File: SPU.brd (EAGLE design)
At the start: 160 x 130 mm, 396 parts, among them Q2 CSTCR6M00G53Z

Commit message: Before autoroute
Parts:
- removed STAMP1:ADC_SG1, STAMP1:ADC_SG2, STAMP1:ADC_TEMP, STAMP2:ADC_SG1, STAMP2:ADC_SG2, STAMP2:ADC_TEMP, STAMP3:ADC_SG1, STAMP3:ADC_SG2, STAMP3:ADC_TEMP, STAMP4:ADC_SG1, STAMP4:ADC_SG2, STAMP4:ADC_TEMP, STAMP5:ADC_SG1, STAMP5:ADC_SG2, STAMP5:ADC_TEMP, STAMP6:ADC_SG1, STAMP6:ADC_SG2, STAMP6:ADC_TEMP: ADS1148QPWRQ1, ads11xx:TSSOP28
- removed STAMP1:C28, STAMP1:C30, STAMP1:C31, STAMP1:C32, STAMP1:C33, STAMP1:C45, STAMP1:C47, STAMP1:C48, STAMP1:C49, STAMP1:C50, STAMP1:C51, STAMP1:C52, STAMP2:C28, STAMP2:C30, STAMP2:C31, STAMP2:C32, STAMP2:C33, STAMP2:C45, STAMP2:C47, STAMP2:C48, STAMP2:C49, STAMP2:C50, STAMP2:C51, STAMP2:C52, STAMP3:C28, STAMP3:C30, STAMP3:C31, STAMP3:C32, STAMP3:C33, STAMP3:C45, STAMP3:C47, STAMP3:C48, STAMP3:C49, STAMP3:C50, STAMP3:C51, STAMP3:C52, STAMP4:C28, STAMP4:C30, STAMP4:C31, STAMP4:C32, STAMP4:C33, STAMP4:C45, STAMP4:C47, STAMP4:C48, STAMP4:C49, STAMP4:C50, STAMP4:C51, STAMP4:C52, STAMP5:C28, STAMP5:C30, STAMP5:C31, STAMP5:C32, STAMP5:C33, STAMP5:C45, STAMP5:C47, STAMP5:C48, STAMP5:C49, STAMP5:C50, STAMP5:C51, STAMP5:C52, STAMP6:C28, STAMP6:C30, STAMP6:C31, STAMP6:C32, STAMP6:C33, STAMP6:C45, STAMP6:C47, STAMP6:C48, STAMP6:C49, STAMP6:C50, STAMP6:C51, STAMP6:C52: 100n, rcl:C0805
- removed STAMP1:C29, STAMP1:C46, STAMP1:C56, STAMP2:C29, STAMP2:C46, STAMP2:C56, STAMP3:C29, STAMP3:C46, STAMP3:C56, STAMP4:C29, STAMP4:C46, STAMP4:C56, STAMP5:C29, STAMP5:C46, STAMP5:C56, STAMP6:C29, STAMP6:C46, STAMP6:C56: 1u, rcl:C0805
- removed STAMP1:C53, STAMP1:C55, STAMP2:C53, STAMP2:C55, STAMP3:C53, STAMP3:C55, STAMP4:C53, STAMP4:C55, STAMP5:C53, STAMP5:C55, STAMP6:C53, STAMP6:C55: 6n8, rcl:C0805
- removed STAMP1:C54, STAMP2:C54, STAMP3:C54, STAMP4:C54, STAMP5:C54, STAMP6:C54: 68n, rcl:C0805
- removed STAMP1:C57, STAMP2:C57, STAMP3:C57, STAMP4:C57, STAMP5:C57, STAMP6:C57: 33n, rcl:C0805
- removed STAMP1:C58, STAMP1:C59, STAMP2:C58, STAMP2:C59, STAMP3:C58, STAMP3:C59, STAMP4:C58, STAMP4:C59, STAMP5:C58, STAMP5:C59, STAMP6:C58, STAMP6:C59: 3n3, rcl:C0805
- removed STAMP1:CON, STAMP2:CON, STAMP3:CON, STAMP4:CON, STAMP5:CON, STAMP6:CON: IL-AG5-10P-S3T2, con-jae:IL-AG5-10P-S3T2
- removed STAMP1:R24, STAMP1:R68, STAMP1:R77, STAMP2:R24, STAMP2:R68, STAMP2:R77, STAMP3:R24, STAMP3:R68, STAMP3:R77, STAMP4:R24, STAMP4:R68, STAMP4:R77, STAMP5:R24, STAMP5:R68, STAMP5:R77, STAMP6:R24, STAMP6:R68, STAMP6:R77: 4k7, rcl:R0805
- removed STAMP1:R29, STAMP1:R32, STAMP1:R72, STAMP1:R73, STAMP2:R29, STAMP2:R32, STAMP2:R72, STAMP2:R73, STAMP3:R29, STAMP3:R32, STAMP3:R72, STAMP3:R73, STAMP4:R29, STAMP4:R32, STAMP4:R72, STAMP4:R73, STAMP5:R29, STAMP5:R32, STAMP5:R72, STAMP5:R73, STAMP6:R29, STAMP6:R32, STAMP6:R72, STAMP6:R73: 40 1%, rcl:R0805
- removed STAMP1:R30, STAMP1:R33, STAMP1:R69, STAMP1:R74, STAMP2:R30, STAMP2:R33, STAMP2:R69, STAMP2:R74, STAMP3:R30, STAMP3:R33, STAMP3:R69, STAMP3:R74, STAMP4:R30, STAMP4:R33, STAMP4:R69, STAMP4:R74, STAMP5:R30, STAMP5:R33, STAMP5:R69, STAMP5:R74, STAMP6:R30, STAMP6:R33, STAMP6:R69, STAMP6:R74: 1k 0.1%, rcl:R0805
- removed STAMP1:R31, STAMP1:R70, STAMP1:R75, STAMP2:R31, STAMP2:R70, STAMP2:R75, STAMP3:R31, STAMP3:R70, STAMP3:R75, STAMP4:R31, STAMP4:R70, STAMP4:R75, STAMP5:R31, STAMP5:R70, STAMP5:R75, STAMP6:R31, STAMP6:R70, STAMP6:R75: 47, rcl:R0805
- removed STAMP1:R78, STAMP1:R79, STAMP2:R78, STAMP2:R79, STAMP3:R78, STAMP3:R79, STAMP4:R78, STAMP4:R79, STAMP5:R78, STAMP5:R79, STAMP6:R78, STAMP6:R79: 4k7 1%, rcl:R0805
- removed STAMP1:R80, STAMP1:R81, STAMP2:R80, STAMP2:R81, STAMP3:R80, STAMP3:R81, STAMP4:R80, STAMP4:R81, STAMP5:R80, STAMP5:R81, STAMP6:R80, STAMP6:R81: 9k09 1%, rcl:R0805
- removed STAMP1:R82, STAMP2:R82, STAMP3:R82, STAMP4:R82, STAMP5:R82, STAMP6:R82: 820 0.1%, rcl:R0805
- removed STAMP1:U$6, STAMP1:U$7, STAMP2:U$6, STAMP2:U$7, STAMP3:U$6, STAMP3:U$7, STAMP4:U$6, STAMP4:U$7, STAMP5:U$6, STAMP5:U$7, STAMP6:U$6, STAMP6:U$7: COMMON_MODE_CHOKE, selfmade:COMMON_MODE_CHOKE
- removed U$1: FT2232D, smf2:FTDI2232D
- removed U$3: M93C46-WDW6TP, smf2:TSSOP-8
- removed U$4: S70FL01GSAGM, smf2:SOIC16
- added C100, C101, C102, C103, C104, C105, C113, C115, C116, C117, C118, C119, C121, C122, C123, C124, C125, C126, C134, C136, C137, C138, C139, C140, C142, C143, C144, C145, C146, C147, C155, C157, C158, C159, C160, C161, C163, C164, C165, C166, C167, C168, C197, C199, C200, C201, C202, C203, C205, C206, C207, C208, C209, C210, C33, C45, C46, C47, C48, C49, C51, C52, C53, C54, C55, C56, C92, C94, C95, C96, C97, C98: 100n, rcl:C0805
- added C106, C108, C127, C129, C148, C150, C169, C171, C211, C213, C57, C59: 6n8, rcl:C0805
- added C107, C128, C149, C170, C212, C58: 68n, rcl:C0805
- added C109, C114, C120, C130, C135, C141, C151, C156, C162, C172, C198, C204, C214, C34, C50, C63, C93, C99: 1u, rcl:C0805
- added C110, C131, C152, C173, C215, C68: 33n, rcl:C0805
- added C111, C112, C132, C133, C153, C154, C174, C175, C216, C217, C69, C70: 3n3, rcl:C0805
- added CON_STAMP1, CON_STAMP3, CON_STAMP4, CON_STAMP5, CON_STAMP6, CON_STAMP8: IL-AG5-10P-S3T2, con-jae:IL-AG5-10P-S3T2
- added FTDI: FT2232D, smf2:FTDI2232D
- added FT_EEPROM: M93C46-WDW6TP, smf2:TSSOP-8
- added R100, R106, R113, R119, R125, R132, R138, R144, R151, R176, R182, R189, R28, R68, R71, R77, R87, R94: 4k7, rcl:R0805
- added R101, R105, R107, R111, R120, R124, R126, R130, R139, R143, R145, R149, R177, R181, R183, R187, R30, R33, R69, R74, R76, R86, R88, R92: 1k 0.1%, rcl:R0805
- added R102, R108, R112, R121, R127, R131, R140, R146, R150, R178, R184, R188, R31, R70, R75, R83, R89, R93: 47, rcl:R0805
- added R103, R104, R109, R110, R122, R123, R128, R129, R141, R142, R147, R148, R179, R180, R185, R186, R29, R32, R72, R73, R84, R85, R90, R91: 40 1%, rcl:R0805
- added R114, R115, R133, R134, R152, R153, R190, R191, R78, R79, R95, R96: 4k7 1%, rcl:R0805
- added R116, R117, R135, R136, R154, R155, R192, R193, R80, R81, R97, R98: 9k09 1%, rcl:R0805
- added R118, R137, R156, R194, R82, R99: 820 0.1%, rcl:R0805
- added S70FL: S70FL01GSAGM, smf2:SOIC16
- added STAMP1_ADC_SG1, STAMP1_ADC_SG10, STAMP1_ADC_SG11, STAMP1_ADC_SG12, STAMP1_ADC_SG15, STAMP1_ADC_SG16, STAMP1_ADC_SG2, STAMP1_ADC_SG5, STAMP1_ADC_SG6, STAMP1_ADC_SG7, STAMP1_ADC_SG8, STAMP1_ADC_SG9, STAMP1_ADC_TEMP, STAMP1_ADC_TEMP2, STAMP1_ADC_TEMP3, STAMP1_ADC_TEMP4, STAMP1_ADC_TEMP5, STAMP1_ADC_TEMP7: ADS1148QPWRQ1, ads11xx:TSSOP28
- added U$10, U$11, U$12, U$13, U$14, U$15, U$16, U$19, U$20, U$6, U$7, U$9: COMMON_MODE_CHOKE, selfmade:COMMON_MODE_CHOKE
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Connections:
- removed net STAMP1:N$34: STAMP1:ADC_SG1.9, STAMP1:C29.1
- removed net STAMP1:N$35: STAMP1:ADC_SG2.4, STAMP1:R68.1
- removed net STAMP1:N$37: STAMP1:ADC_SG1.4, STAMP1:R24.1
- removed net STAMP1:N$38: STAMP1:ADC_SG1.26, STAMP1:R31.2
- removed net STAMP1:N$39: STAMP1:ADC_SG1.11, STAMP1:C31.2, STAMP1:C32.1, STAMP1:R29.1
- removed net STAMP1:N$40: STAMP1:ADC_SG1.12, STAMP1:C32.2, STAMP1:C33.1, STAMP1:R32.1
- removed net STAMP1:N$41: STAMP1:ADC_SG2.9, STAMP1:C46.1
- removed net STAMP1:N$43: STAMP1:ADC_SG2.26, STAMP1:R70.2
- removed net STAMP1:N$79: STAMP1:ADC_SG2.11, STAMP1:C48.2, STAMP1:C49.1, STAMP1:R72.1
- removed net STAMP1:N$80: STAMP1:ADC_SG2.12, STAMP1:C49.2, STAMP1:C50.1, STAMP1:R73.1
- removed net STAMP1:N$81: STAMP1:R30.1, STAMP1:R32.2, STAMP1:R33.1
- removed net STAMP1:N$82: STAMP1:R69.1, STAMP1:R73.2, STAMP1:R74.1
- removed net STAMP1:N$83: STAMP1:R29.2, STAMP1:U$6.P$3
- removed net STAMP1:N$84: STAMP1:R72.2, STAMP1:U$7.P$3
- removed net STAMP1:N$86: STAMP1:ADC_TEMP.26, STAMP1:R75.2
- removed net STAMP1:N$87: STAMP1:ADC_TEMP.4, STAMP1:R77.1
- removed net STAMP1:N$88: STAMP1:ADC_TEMP.12, STAMP1:C53.2, STAMP1:C54.1, STAMP1:R78.1
- removed net STAMP1:N$89: STAMP1:ADC_TEMP.17, STAMP1:C54.2, STAMP1:C55.1, STAMP1:R79.1
- removed net STAMP1:N$90: STAMP1:ADC_TEMP.9, STAMP1:C56.1
- removed net STAMP1:N$91: STAMP1:ADC_TEMP.6, STAMP1:C57.2, STAMP1:C58.1, STAMP1:R81.1
- removed net STAMP1:N$92: STAMP1:ADC_TEMP.5, STAMP1:C57.1, STAMP1:C59.2, STAMP1:R80.1
- removed net STAMP1:SG1_AIN1: STAMP1:CON.P$1, STAMP1:U$6.P$6
- removed net STAMP1:SG1_AIN2: STAMP1:CON.P$2, STAMP1:U$6.P$4
- removed net STAMP1:SG1_AIN3: STAMP1:CON.P$3, STAMP1:U$6.P$2
- removed net STAMP1:SG2_AIN1: STAMP1:CON.P$10, STAMP1:U$7.P$6
- removed net STAMP1:SG2_AIN2: STAMP1:CON.P$9, STAMP1:U$7.P$4
- removed net STAMP1:SG2_AIN3: STAMP1:CON.P$8, STAMP1:U$7.P$2
- removed net STAMP1:TEMP_AIN1: STAMP1:ADC_TEMP.11, STAMP1:CON.P$4, STAMP1:R78.2
- removed net STAMP1:TEMP_AIN2: STAMP1:ADC_TEMP.18, STAMP1:CON.P$5, STAMP1:R79.2
- removed net STAMP1:TEMP_AIN3: STAMP1:CON.P$7, STAMP1:R80.2, STAMP1:R82.2
- removed net STAMP2:N$34: STAMP2:ADC_SG1.9, STAMP2:C29.1
- removed net STAMP2:N$35: STAMP2:ADC_SG2.4, STAMP2:R68.1
- removed net STAMP2:N$37: STAMP2:ADC_SG1.4, STAMP2:R24.1
- removed net STAMP2:N$38: STAMP2:ADC_SG1.26, STAMP2:R31.2
- removed net STAMP2:N$39: STAMP2:ADC_SG1.11, STAMP2:C31.2, STAMP2:C32.1, STAMP2:R29.1
- removed net STAMP2:N$40: STAMP2:ADC_SG1.12, STAMP2:C32.2, STAMP2:C33.1, STAMP2:R32.1
- removed net STAMP2:N$41: STAMP2:ADC_SG2.9, STAMP2:C46.1
- removed net STAMP2:N$43: STAMP2:ADC_SG2.26, STAMP2:R70.2
- removed net STAMP2:N$79: STAMP2:ADC_SG2.11, STAMP2:C48.2, STAMP2:C49.1, STAMP2:R72.1
- removed net STAMP2:N$80: STAMP2:ADC_SG2.12, STAMP2:C49.2, STAMP2:C50.1, STAMP2:R73.1
- removed net STAMP2:N$81: STAMP2:R30.1, STAMP2:R32.2, STAMP2:R33.1
- removed net STAMP2:N$82: STAMP2:R69.1, STAMP2:R73.2, STAMP2:R74.1
- removed net STAMP2:N$83: STAMP2:R29.2, STAMP2:U$6.P$3
- removed net STAMP2:N$84: STAMP2:R72.2, STAMP2:U$7.P$3
- removed net STAMP2:N$86: STAMP2:ADC_TEMP.26, STAMP2:R75.2
- removed net STAMP2:N$87: STAMP2:ADC_TEMP.4, STAMP2:R77.1
- removed net STAMP2:N$88: STAMP2:ADC_TEMP.12, STAMP2:C53.2, STAMP2:C54.1, STAMP2:R78.1
- removed net STAMP2:N$89: STAMP2:ADC_TEMP.17, STAMP2:C54.2, STAMP2:C55.1, STAMP2:R79.1
- removed net STAMP2:N$90: STAMP2:ADC_TEMP.9, STAMP2:C56.1
- removed net STAMP2:N$91: STAMP2:ADC_TEMP.6, STAMP2:C57.2, STAMP2:C58.1, STAMP2:R81.1
- removed net STAMP2:N$92: STAMP2:ADC_TEMP.5, STAMP2:C57.1, STAMP2:C59.2, STAMP2:R80.1
- removed net STAMP2:SG1_AIN1: STAMP2:CON.P$1, STAMP2:U$6.P$6
- removed net STAMP2:SG1_AIN2: STAMP2:CON.P$2, STAMP2:U$6.P$4
- removed net STAMP2:SG1_AIN3: STAMP2:CON.P$3, STAMP2:U$6.P$2
- removed net STAMP2:SG2_AIN1: STAMP2:CON.P$10, STAMP2:U$7.P$6
- removed net STAMP2:SG2_AIN2: STAMP2:CON.P$9, STAMP2:U$7.P$4
- removed net STAMP2:SG2_AIN3: STAMP2:CON.P$8, STAMP2:U$7.P$2
- removed net STAMP2:TEMP_AIN1: STAMP2:ADC_TEMP.11, STAMP2:CON.P$4, STAMP2:R78.2
- removed net STAMP2:TEMP_AIN2: STAMP2:ADC_TEMP.18, STAMP2:CON.P$5, STAMP2:R79.2
- removed net STAMP2:TEMP_AIN3: STAMP2:CON.P$7, STAMP2:R80.2, STAMP2:R82.2
- removed net STAMP3:N$34: STAMP3:ADC_SG1.9, STAMP3:C29.1
- removed net STAMP3:N$35: STAMP3:ADC_SG2.4, STAMP3:R68.1
- removed net STAMP3:N$37: STAMP3:ADC_SG1.4, STAMP3:R24.1
- removed net STAMP3:N$38: STAMP3:ADC_SG1.26, STAMP3:R31.2
- removed net STAMP3:N$39: STAMP3:ADC_SG1.11, STAMP3:C31.2, STAMP3:C32.1, STAMP3:R29.1
- removed net STAMP3:N$40: STAMP3:ADC_SG1.12, STAMP3:C32.2, STAMP3:C33.1, STAMP3:R32.1
- removed net STAMP3:N$41: STAMP3:ADC_SG2.9, STAMP3:C46.1
- removed net STAMP3:N$43: STAMP3:ADC_SG2.26, STAMP3:R70.2
- removed net STAMP3:N$79: STAMP3:ADC_SG2.11, STAMP3:C48.2, STAMP3:C49.1, STAMP3:R72.1
- removed net STAMP3:N$80: STAMP3:ADC_SG2.12, STAMP3:C49.2, STAMP3:C50.1, STAMP3:R73.1
- removed net STAMP3:N$81: STAMP3:R30.1, STAMP3:R32.2, STAMP3:R33.1
- removed net STAMP3:N$82: STAMP3:R69.1, STAMP3:R73.2, STAMP3:R74.1
- removed net STAMP3:N$83: STAMP3:R29.2, STAMP3:U$6.P$3
- removed net STAMP3:N$84: STAMP3:R72.2, STAMP3:U$7.P$3
- removed net STAMP3:N$86: STAMP3:ADC_TEMP.26, STAMP3:R75.2
- removed net STAMP3:N$87: STAMP3:ADC_TEMP.4, STAMP3:R77.1
- removed net STAMP3:N$88: STAMP3:ADC_TEMP.12, STAMP3:C53.2, STAMP3:C54.1, STAMP3:R78.1
- removed net STAMP3:N$89: STAMP3:ADC_TEMP.17, STAMP3:C54.2, STAMP3:C55.1, STAMP3:R79.1
- removed net STAMP3:N$90: STAMP3:ADC_TEMP.9, STAMP3:C56.1
- removed net STAMP3:N$91: STAMP3:ADC_TEMP.6, STAMP3:C57.2, STAMP3:C58.1, STAMP3:R81.1
- removed net STAMP3:N$92: STAMP3:ADC_TEMP.5, STAMP3:C57.1, STAMP3:C59.2, STAMP3:R80.1
- removed net STAMP3:SG1_AIN1: STAMP3:CON.P$1, STAMP3:U$6.P$6
- removed net STAMP3:SG1_AIN2: STAMP3:CON.P$2, STAMP3:U$6.P$4
- removed net STAMP3:SG1_AIN3: STAMP3:CON.P$3, STAMP3:U$6.P$2
- removed net STAMP3:SG2_AIN1: STAMP3:CON.P$10, STAMP3:U$7.P$6
- removed net STAMP3:SG2_AIN2: STAMP3:CON.P$9, STAMP3:U$7.P$4
- removed net STAMP3:SG2_AIN3: STAMP3:CON.P$8, STAMP3:U$7.P$2
- removed net STAMP3:TEMP_AIN1: STAMP3:ADC_TEMP.11, STAMP3:CON.P$4, STAMP3:R78.2
- removed net STAMP3:TEMP_AIN2: STAMP3:ADC_TEMP.18, STAMP3:CON.P$5, STAMP3:R79.2
- removed net STAMP3:TEMP_AIN3: STAMP3:CON.P$7, STAMP3:R80.2, STAMP3:R82.2
- removed net STAMP4:N$34: STAMP4:ADC_SG1.9, STAMP4:C29.1
- removed net STAMP4:N$35: STAMP4:ADC_SG2.4, STAMP4:R68.1
- removed net STAMP4:N$37: STAMP4:ADC_SG1.4, STAMP4:R24.1
- removed net STAMP4:N$38: STAMP4:ADC_SG1.26, STAMP4:R31.2
- removed net STAMP4:N$39: STAMP4:ADC_SG1.11, STAMP4:C31.2, STAMP4:C32.1, STAMP4:R29.1
- removed net STAMP4:N$40: STAMP4:ADC_SG1.12, STAMP4:C32.2, STAMP4:C33.1, STAMP4:R32.1
- removed net STAMP4:N$41: STAMP4:ADC_SG2.9, STAMP4:C46.1
- removed net STAMP4:N$43: STAMP4:ADC_SG2.26, STAMP4:R70.2
- removed net STAMP4:N$79: STAMP4:ADC_SG2.11, STAMP4:C48.2, STAMP4:C49.1, STAMP4:R72.1
- removed net STAMP4:N$80: STAMP4:ADC_SG2.12, STAMP4:C49.2, STAMP4:C50.1, STAMP4:R73.1
- removed net STAMP4:N$81: STAMP4:R30.1, STAMP4:R32.2, STAMP4:R33.1
- removed net STAMP4:N$82: STAMP4:R69.1, STAMP4:R73.2, STAMP4:R74.1
- removed net STAMP4:N$83: STAMP4:R29.2, STAMP4:U$6.P$3
- removed net STAMP4:N$84: STAMP4:R72.2, STAMP4:U$7.P$3
- removed net STAMP4:N$86: STAMP4:ADC_TEMP.26, STAMP4:R75.2
- removed net STAMP4:N$87: STAMP4:ADC_TEMP.4, STAMP4:R77.1
- removed net STAMP4:N$88: STAMP4:ADC_TEMP.12, STAMP4:C53.2, STAMP4:C54.1, STAMP4:R78.1
- removed net STAMP4:N$89: STAMP4:ADC_TEMP.17, STAMP4:C54.2, STAMP4:C55.1, STAMP4:R79.1
- removed net STAMP4:N$90: STAMP4:ADC_TEMP.9, STAMP4:C56.1
- removed net STAMP4:N$91: STAMP4:ADC_TEMP.6, STAMP4:C57.2, STAMP4:C58.1, STAMP4:R81.1
- removed net STAMP4:N$92: STAMP4:ADC_TEMP.5, STAMP4:C57.1, STAMP4:C59.2, STAMP4:R80.1
- removed net STAMP4:SG1_AIN1: STAMP4:CON.P$1, STAMP4:U$6.P$6
- removed net STAMP4:SG1_AIN2: STAMP4:CON.P$2, STAMP4:U$6.P$4
- removed net STAMP4:SG1_AIN3: STAMP4:CON.P$3, STAMP4:U$6.P$2
- removed net STAMP4:SG2_AIN1: STAMP4:CON.P$10, STAMP4:U$7.P$6
- removed net STAMP4:SG2_AIN2: STAMP4:CON.P$9, STAMP4:U$7.P$4
- removed net STAMP4:SG2_AIN3: STAMP4:CON.P$8, STAMP4:U$7.P$2
- removed net STAMP4:TEMP_AIN1: STAMP4:ADC_TEMP.11, STAMP4:CON.P$4, STAMP4:R78.2
- removed net STAMP4:TEMP_AIN2: STAMP4:ADC_TEMP.18, STAMP4:CON.P$5, STAMP4:R79.2
- removed net STAMP4:TEMP_AIN3: STAMP4:CON.P$7, STAMP4:R80.2, STAMP4:R82.2
- removed net STAMP5:N$34: STAMP5:ADC_SG1.9, STAMP5:C29.1
- removed net STAMP5:N$35: STAMP5:ADC_SG2.4, STAMP5:R68.1
- removed net STAMP5:N$37: STAMP5:ADC_SG1.4, STAMP5:R24.1
- removed net STAMP5:N$38: STAMP5:ADC_SG1.26, STAMP5:R31.2
- removed net STAMP5:N$39: STAMP5:ADC_SG1.11, STAMP5:C31.2, STAMP5:C32.1, STAMP5:R29.1
- removed net STAMP5:N$40: STAMP5:ADC_SG1.12, STAMP5:C32.2, STAMP5:C33.1, STAMP5:R32.1
- removed net STAMP5:N$41: STAMP5:ADC_SG2.9, STAMP5:C46.1
- removed net STAMP5:N$43: STAMP5:ADC_SG2.26, STAMP5:R70.2
- removed net STAMP5:N$79: STAMP5:ADC_SG2.11, STAMP5:C48.2, STAMP5:C49.1, STAMP5:R72.1
- removed net STAMP5:N$80: STAMP5:ADC_SG2.12, STAMP5:C49.2, STAMP5:C50.1, STAMP5:R73.1
- removed net STAMP5:N$81: STAMP5:R30.1, STAMP5:R32.2, STAMP5:R33.1
- removed net STAMP5:N$82: STAMP5:R69.1, STAMP5:R73.2, STAMP5:R74.1
- removed net STAMP5:N$83: STAMP5:R29.2, STAMP5:U$6.P$3
- removed net STAMP5:N$84: STAMP5:R72.2, STAMP5:U$7.P$3
- removed net STAMP5:N$86: STAMP5:ADC_TEMP.26, STAMP5:R75.2
- removed net STAMP5:N$87: STAMP5:ADC_TEMP.4, STAMP5:R77.1
- removed net STAMP5:N$88: STAMP5:ADC_TEMP.12, STAMP5:C53.2, STAMP5:C54.1, STAMP5:R78.1
- removed net STAMP5:N$89: STAMP5:ADC_TEMP.17, STAMP5:C54.2, STAMP5:C55.1, STAMP5:R79.1
- removed net STAMP5:N$90: STAMP5:ADC_TEMP.9, STAMP5:C56.1
- removed net STAMP5:N$91: STAMP5:ADC_TEMP.6, STAMP5:C57.2, STAMP5:C58.1, STAMP5:R81.1
- removed net STAMP5:N$92: STAMP5:ADC_TEMP.5, STAMP5:C57.1, STAMP5:C59.2, STAMP5:R80.1
- removed net STAMP5:SG1_AIN1: STAMP5:CON.P$1, STAMP5:U$6.P$6
- removed net STAMP5:SG1_AIN2: STAMP5:CON.P$2, STAMP5:U$6.P$4
- removed net STAMP5:SG1_AIN3: STAMP5:CON.P$3, STAMP5:U$6.P$2
- removed net STAMP5:SG2_AIN1: STAMP5:CON.P$10, STAMP5:U$7.P$6
- removed net STAMP5:SG2_AIN2: STAMP5:CON.P$9, STAMP5:U$7.P$4
- removed net STAMP5:SG2_AIN3: STAMP5:CON.P$8, STAMP5:U$7.P$2
- removed net STAMP5:TEMP_AIN1: STAMP5:ADC_TEMP.11, STAMP5:CON.P$4, STAMP5:R78.2
- removed net STAMP5:TEMP_AIN2: STAMP5:ADC_TEMP.18, STAMP5:CON.P$5, STAMP5:R79.2
- removed net STAMP5:TEMP_AIN3: STAMP5:CON.P$7, STAMP5:R80.2, STAMP5:R82.2
- removed net STAMP6:N$34: STAMP6:ADC_SG1.9, STAMP6:C29.1
- removed net STAMP6:N$35: STAMP6:ADC_SG2.4, STAMP6:R68.1
- removed net STAMP6:N$37: STAMP6:ADC_SG1.4, STAMP6:R24.1
- removed net STAMP6:N$38: STAMP6:ADC_SG1.26, STAMP6:R31.2
- removed net STAMP6:N$39: STAMP6:ADC_SG1.11, STAMP6:C31.2, STAMP6:C32.1, STAMP6:R29.1
- removed net STAMP6:N$40: STAMP6:ADC_SG1.12, STAMP6:C32.2, STAMP6:C33.1, STAMP6:R32.1
- removed net STAMP6:N$41: STAMP6:ADC_SG2.9, STAMP6:C46.1
- removed net STAMP6:N$43: STAMP6:ADC_SG2.26, STAMP6:R70.2
- removed net STAMP6:N$79: STAMP6:ADC_SG2.11, STAMP6:C48.2, STAMP6:C49.1, STAMP6:R72.1
- removed net STAMP6:N$80: STAMP6:ADC_SG2.12, STAMP6:C49.2, STAMP6:C50.1, STAMP6:R73.1
- removed net STAMP6:N$81: STAMP6:R30.1, STAMP6:R32.2, STAMP6:R33.1
- removed net STAMP6:N$82: STAMP6:R69.1, STAMP6:R73.2, STAMP6:R74.1
- removed net STAMP6:N$83: STAMP6:R29.2, STAMP6:U$6.P$3
- removed net STAMP6:N$84: STAMP6:R72.2, STAMP6:U$7.P$3
- removed net STAMP6:N$86: STAMP6:ADC_TEMP.26, STAMP6:R75.2
- removed net STAMP6:N$87: STAMP6:ADC_TEMP.4, STAMP6:R77.1
- removed net STAMP6:N$88: STAMP6:ADC_TEMP.12, STAMP6:C53.2, STAMP6:C54.1, STAMP6:R78.1
- removed net STAMP6:N$89: STAMP6:ADC_TEMP.17, STAMP6:C54.2, STAMP6:C55.1, STAMP6:R79.1
- removed net STAMP6:N$90: STAMP6:ADC_TEMP.9, STAMP6:C56.1
- removed net STAMP6:N$91: STAMP6:ADC_TEMP.6, STAMP6:C57.2, STAMP6:C58.1, STAMP6:R81.1
- removed net STAMP6:N$92: STAMP6:ADC_TEMP.5, STAMP6:C57.1, STAMP6:C59.2, STAMP6:R80.1
- removed net STAMP6:SG1_AIN1: STAMP6:CON.P$1, STAMP6:U$6.P$6
- removed net STAMP6:SG1_AIN2: STAMP6:CON.P$2, STAMP6:U$6.P$4
- removed net STAMP6:SG1_AIN3: STAMP6:CON.P$3, STAMP6:U$6.P$2
- removed net STAMP6:SG2_AIN1: STAMP6:CON.P$10, STAMP6:U$7.P$6
- removed net STAMP6:SG2_AIN2: STAMP6:CON.P$9, STAMP6:U$7.P$4
- removed net STAMP6:SG2_AIN3: STAMP6:CON.P$8, STAMP6:U$7.P$2
- removed net STAMP6:TEMP_AIN1: STAMP6:ADC_TEMP.11, STAMP6:CON.P$4, STAMP6:R78.2
- removed net STAMP6:TEMP_AIN2: STAMP6:ADC_TEMP.18, STAMP6:CON.P$5, STAMP6:R79.2
- removed net STAMP6:TEMP_AIN3: STAMP6:CON.P$7, STAMP6:R80.2, STAMP6:R82.2
- new net N$100: R89.2, STAMP1_ADC_SG6.26
- new net N$101: C101.2, C102.1, R90.1, STAMP1_ADC_SG6.11
- new net N$102: C102.2, C103.1, R91.1, STAMP1_ADC_SG6.12
- new net N$103: R88.1, R91.2, R92.1
- new net N$104: R90.2, U$10.P$3
- new net N$105: R93.2, STAMP1_ADC_TEMP2.26
- new net N$106: R94.1, STAMP1_ADC_TEMP2.4
- new net N$107: C106.2, C107.1, R95.1, STAMP1_ADC_TEMP2.12
- new net N$108: C107.2, C108.1, R96.1, STAMP1_ADC_TEMP2.17
- new net N$109: C109.1, STAMP1_ADC_TEMP2.9
- new net N$110: C110.2, C111.1, R98.1, STAMP1_ADC_TEMP2.6
- new net N$111: C110.1, C112.2, R97.1, STAMP1_ADC_TEMP2.5
- new net N$112: R100.1, STAMP1_ADC_SG7.4
- new net N$113: C114.1, STAMP1_ADC_SG7.9
- new net N$114: R102.2, STAMP1_ADC_SG7.26
- new net N$115: C116.2, C117.1, R103.1, STAMP1_ADC_SG7.11
- new net N$116: C117.2, C118.1, R104.1, STAMP1_ADC_SG7.12
- new net N$117: R101.1, R104.2, R105.1
- new net N$118: R103.2, U$11.P$3
- new net N$119: R106.1, STAMP1_ADC_SG8.4
- new net N$120: C120.1, STAMP1_ADC_SG8.9
- new net N$121: R108.2, STAMP1_ADC_SG8.26
- new net N$122: C122.2, C123.1, R109.1, STAMP1_ADC_SG8.11
- new net N$123: C123.2, C124.1, R110.1, STAMP1_ADC_SG8.12
- new net N$124: R107.1, R110.2, R111.1
- new net N$125: R109.2, U$12.P$3
- new net N$126: R112.2, STAMP1_ADC_TEMP3.26
- new net N$127: R113.1, STAMP1_ADC_TEMP3.4
- new net N$128: C127.2, C128.1, R114.1, STAMP1_ADC_TEMP3.12
- new net N$129: C128.2, C129.1, R115.1, STAMP1_ADC_TEMP3.17
- new net N$130: C130.1, STAMP1_ADC_TEMP3.9
- new net N$131: C131.2, C132.1, R117.1, STAMP1_ADC_TEMP3.6
- new net N$132: C131.1, C133.2, R116.1, STAMP1_ADC_TEMP3.5
- new net N$133: R119.1, STAMP1_ADC_SG9.4
- new net N$134: C135.1, STAMP1_ADC_SG9.9
- new net N$135: R121.2, STAMP1_ADC_SG9.26
- new net N$136: C137.2, C138.1, R122.1, STAMP1_ADC_SG9.11
- new net N$137: C138.2, C139.1, R123.1, STAMP1_ADC_SG9.12
- new net N$138: R120.1, R123.2, R124.1
- new net N$139: R122.2, U$13.P$3
- new net N$140: R125.1, STAMP1_ADC_SG10.4
- new net N$141: C141.1, STAMP1_ADC_SG10.9
- new net N$142: R127.2, STAMP1_ADC_SG10.26
- new net N$143: C143.2, C144.1, R128.1, STAMP1_ADC_SG10.11
- new net N$144: C144.2, C145.1, R129.1, STAMP1_ADC_SG10.12
- new net N$145: R126.1, R129.2, R130.1
- new net N$146: R128.2, U$14.P$3
- new net N$147: R131.2, STAMP1_ADC_TEMP4.26
- new net N$148: R132.1, STAMP1_ADC_TEMP4.4
- new net N$149: C148.2, C149.1, R133.1, STAMP1_ADC_TEMP4.12
- new net N$150: C149.2, C150.1, R134.1, STAMP1_ADC_TEMP4.17
- new net N$151: C151.1, STAMP1_ADC_TEMP4.9
- new net N$152: C152.2, C153.1, R136.1, STAMP1_ADC_TEMP4.6
- new net N$153: C152.1, C154.2, R135.1, STAMP1_ADC_TEMP4.5
- new net N$154: R138.1, STAMP1_ADC_SG11.4
- new net N$155: C156.1, STAMP1_ADC_SG11.9
- new net N$156: R140.2, STAMP1_ADC_SG11.26
- new net N$157: C158.2, C159.1, R141.1, STAMP1_ADC_SG11.11
- new net N$158: C159.2, C160.1, R142.1, STAMP1_ADC_SG11.12
- new net N$159: R139.1, R142.2, R143.1
- new net N$160: R141.2, U$15.P$3
- new net N$161: R144.1, STAMP1_ADC_SG12.4
- new net N$162: C162.1, STAMP1_ADC_SG12.9
- new net N$163: R146.2, STAMP1_ADC_SG12.26
- new net N$164: C164.2, C165.1, R147.1, STAMP1_ADC_SG12.11
- new net N$165: C165.2, C166.1, R148.1, STAMP1_ADC_SG12.12
- new net N$166: R145.1, R148.2, R149.1
- new net N$167: R147.2, U$16.P$3
- new net N$168: R150.2, STAMP1_ADC_TEMP5.26
- new net N$169: R151.1, STAMP1_ADC_TEMP5.4
- new net N$170: C169.2, C170.1, R152.1, STAMP1_ADC_TEMP5.12
- new net N$171: C170.2, C171.1, R153.1, STAMP1_ADC_TEMP5.17
- new net N$172: C172.1, STAMP1_ADC_TEMP5.9
- new net N$173: C173.2, C174.1, R155.1, STAMP1_ADC_TEMP5.6
- new net N$174: C173.1, C175.2, R154.1, STAMP1_ADC_TEMP5.5
- new net N$196: R176.1, STAMP1_ADC_SG15.4
- new net N$197: C198.1, STAMP1_ADC_SG15.9
- new net N$198: R178.2, STAMP1_ADC_SG15.26
- new net N$199: C200.2, C201.1, R179.1, STAMP1_ADC_SG15.11
- new net N$200: C201.2, C202.1, R180.1, STAMP1_ADC_SG15.12
- new net N$201: R177.1, R180.2, R181.1
- new net N$202: R179.2, U$19.P$3
- new net N$203: R182.1, STAMP1_ADC_SG16.4
- new net N$204: C204.1, STAMP1_ADC_SG16.9
- new net N$205: R184.2, STAMP1_ADC_SG16.26
- new net N$206: C206.2, C207.1, R185.1, STAMP1_ADC_SG16.11
- new net N$207: C207.2, C208.1, R186.1, STAMP1_ADC_SG16.12
- new net N$208: R183.1, R186.2, R187.1
- new net N$209: R185.2, U$20.P$3
- new net N$210: R188.2, STAMP1_ADC_TEMP7.26
- new net N$211: R189.1, STAMP1_ADC_TEMP7.4
- new net N$212: C211.2, C212.1, R190.1, STAMP1_ADC_TEMP7.12
- new net N$213: C212.2, C213.1, R191.1, STAMP1_ADC_TEMP7.17
- new net N$214: C214.1, STAMP1_ADC_TEMP7.9
- new net N$215: C215.2, C216.1, R193.1, STAMP1_ADC_TEMP7.6
- new net N$216: C215.1, C217.2, R192.1, STAMP1_ADC_TEMP7.5
- new net N$34: C34.1, STAMP1_ADC_SG1.9
- new net N$35: R68.1, STAMP1_ADC_SG2.4
- new net N$37: R28.1, STAMP1_ADC_SG1.4
- new net N$38: R31.2, STAMP1_ADC_SG1.26
- new net N$39: C46.2, C47.1, R29.1, STAMP1_ADC_SG1.11
- new net N$40: C47.2, C48.1, R32.1, STAMP1_ADC_SG1.12
- new net N$41: C50.1, STAMP1_ADC_SG2.9
- new net N$43: R70.2, STAMP1_ADC_SG2.26
- new net N$78: R71.1, STAMP1_ADC_SG5.4
- new net N$79: C52.2, C53.1, R72.1, STAMP1_ADC_SG2.11
- new net N$80: C53.2, C54.1, R73.1, STAMP1_ADC_SG2.12
- new net N$81: R30.1, R32.2, R33.1
- new net N$82: R69.1, R73.2, R74.1
- new net N$83: R29.2, U$6.P$3
- new net N$84: R72.2, U$7.P$3
- new net N$85: C93.1, STAMP1_ADC_SG5.9
- new net N$86: R75.2, STAMP1_ADC_TEMP.26
- new net N$87: R77.1, STAMP1_ADC_TEMP.4
- new net N$88: C57.2, C58.1, R78.1, STAMP1_ADC_TEMP.12
- new net N$89: C58.2, C59.1, R79.1, STAMP1_ADC_TEMP.17
- new net N$90: C63.1, STAMP1_ADC_TEMP.9
- new net N$91: C68.2, C69.1, R81.1, STAMP1_ADC_TEMP.6
- new net N$92: C68.1, C70.2, R80.1, STAMP1_ADC_TEMP.5
- new net N$93: R83.2, STAMP1_ADC_SG5.26
- new net N$94: C95.2, C96.1, R84.1, STAMP1_ADC_SG5.11
- new net N$95: C96.2, C97.1, R85.1, STAMP1_ADC_SG5.12
- new net N$96: R76.1, R85.2, R86.1
- new net N$97: R84.2, U$9.P$3
- new net N$98: R87.1, STAMP1_ADC_SG6.4
- new net N$99: C99.1, STAMP1_ADC_SG6.9
- new net STAMP1_SG1_AIN1: CON_STAMP1.P$1, U$6.P$6
- new net STAMP1_SG1_AIN2: CON_STAMP1.P$2, U$6.P$4
- new net STAMP1_SG1_AIN3: CON_STAMP1.P$3, U$6.P$2
- new net STAMP1_SG2_AIN1: CON_STAMP1.P$10, U$7.P$6
- new net STAMP1_SG2_AIN2: CON_STAMP1.P$9, U$7.P$4
- new net STAMP1_SG2_AIN3: CON_STAMP1.P$8, U$7.P$2
- new net STAMP1_TEMP_AIN1: CON_STAMP1.P$4, R78.2, STAMP1_ADC_TEMP.11
- new net STAMP1_TEMP_AIN2: CON_STAMP1.P$5, R79.2, STAMP1_ADC_TEMP.18
- new net STAMP1_TEMP_AIN3: CON_STAMP1.P$6, R80.2, R82.2
- new net STAMP2_SG1_AIN1: CON_STAMP3.P$1, U$9.P$6
- new net STAMP2_SG1_AIN2: CON_STAMP3.P$2, U$9.P$4
- new net STAMP2_SG1_AIN3: CON_STAMP3.P$3, U$9.P$2
- new net STAMP2_SG2_AIN1: CON_STAMP3.P$10, U$10.P$6
- new net STAMP2_SG2_AIN2: CON_STAMP3.P$9, U$10.P$4
- new net STAMP2_SG2_AIN3: CON_STAMP3.P$8, U$10.P$2
- new net STAMP2_TEMP_AIN1: CON_STAMP3.P$4, R95.2, STAMP1_ADC_TEMP2.11
- new net STAMP2_TEMP_AIN2: CON_STAMP3.P$5, R96.2, STAMP1_ADC_TEMP2.18
- new net STAMP2_TEMP_AIN3: CON_STAMP3.P$6, R97.2, R99.2
- new net STAMP3_SG1_AIN1: CON_STAMP5.P$1, U$13.P$6
- new net STAMP3_SG1_AIN2: CON_STAMP5.P$2, U$13.P$4
- new net STAMP3_SG1_AIN3: CON_STAMP5.P$3, U$13.P$2
- new net STAMP3_SG2_AIN1: CON_STAMP5.P$10, U$14.P$6
- new net STAMP3_SG2_AIN2: CON_STAMP5.P$9, U$14.P$4
- new net STAMP3_SG2_AIN3: CON_STAMP5.P$8, U$14.P$2
- new net STAMP3_TEMP_AIN1: CON_STAMP5.P$4, R133.2, STAMP1_ADC_TEMP4.11
- new net STAMP3_TEMP_AIN2: CON_STAMP5.P$5, R134.2, STAMP1_ADC_TEMP4.18
- new net STAMP3_TEMP_AIN3: CON_STAMP5.P$6, R135.2, R137.2
- new net STAMP4_SG1_AIN1: CON_STAMP6.P$1, U$15.P$6
- new net STAMP4_SG1_AIN2: CON_STAMP6.P$2, U$15.P$4
- new net STAMP4_SG1_AIN3: CON_STAMP6.P$3, U$15.P$2
- new net STAMP4_SG2_AIN1: CON_STAMP6.P$10, U$16.P$6
- new net STAMP4_SG2_AIN2: CON_STAMP6.P$9, U$16.P$4
- new net STAMP4_SG2_AIN3: CON_STAMP6.P$8, U$16.P$2
- new net STAMP4_TEMP_AIN1: CON_STAMP6.P$4, R152.2, STAMP1_ADC_TEMP5.11
- new net STAMP4_TEMP_AIN2: CON_STAMP6.P$5, R153.2, STAMP1_ADC_TEMP5.18
- new net STAMP4_TEMP_AIN3: CON_STAMP6.P$6, R154.2, R156.2
- new net STAMP5_SG1_AIN1: CON_STAMP4.P$1, U$11.P$6
- new net STAMP5_SG1_AIN2: CON_STAMP4.P$2, U$11.P$4
- new net STAMP5_SG1_AIN3: CON_STAMP4.P$3, U$11.P$2
- new net STAMP5_SG2_AIN1: CON_STAMP4.P$10, U$12.P$6
- new net STAMP5_SG2_AIN2: CON_STAMP4.P$9, U$12.P$4
- new net STAMP5_SG2_AIN3: CON_STAMP4.P$8, U$12.P$2
- new net STAMP5_TEMP_AIN1: CON_STAMP4.P$4, R114.2, STAMP1_ADC_TEMP3.11
- new net STAMP5_TEMP_AIN2: CON_STAMP4.P$5, R115.2, STAMP1_ADC_TEMP3.18
- new net STAMP5_TEMP_AIN3: CON_STAMP4.P$6, R116.2, R118.2
- new net STAMP6_SG1_AIN1: CON_STAMP8.P$1, U$19.P$6
- new net STAMP6_SG1_AIN2: CON_STAMP8.P$2, U$19.P$4
- new net STAMP6_SG1_AIN3: CON_STAMP8.P$3, U$19.P$2
- new net STAMP6_SG2_AIN1: CON_STAMP8.P$10, U$20.P$6
- new net STAMP6_SG2_AIN2: CON_STAMP8.P$9, U$20.P$4
- new net STAMP6_SG2_AIN3: CON_STAMP8.P$8, U$20.P$2
- new net STAMP6_TEMP_AIN1: CON_STAMP8.P$4, R190.2, STAMP1_ADC_TEMP7.11
- new net STAMP6_TEMP_AIN2: CON_STAMP8.P$5, R191.2, STAMP1_ADC_TEMP7.18
- new net STAMP6_TEMP_AIN3: CON_STAMP8.P$6, R192.2, R194.2
- net 3V3: now also C100.1, C104.1, C105.1, C113.1, C115.1, C119.1, C121.1, C125.1, C126.1, C134.1, C136.1, C140.1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; no longer STAMP1:ADC_SG1.1, STAMP1:ADC_SG1.22, STAMP1:ADC_SG2.1, STAMP1:ADC_SG2.22, STAMP1:ADC_TEMP.1, STAMP1:ADC_TEMP.22, STAMP1:C28.1, STAMP1:C30.1, STAMP1:C45.1, STAMP1:C47.1, STAMP1:C51.1, STAMP1:C52.1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
- net ADC_START: now also STAMP1_ADC_SG1.23, STAMP1_ADC_SG10.23, STAMP1_ADC_SG11.23, STAMP1_ADC_SG12.23, STAMP1_ADC_SG15.23, STAMP1_ADC_SG16.23, STAMP1_ADC_SG2.23, STAMP1_ADC_SG5.23, STAMP1_ADC_SG6.23, STAMP1_ADC_SG7.23, STAMP1_ADC_SG8.23, STAMP1_ADC_SG9.23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; no longer STAMP1:ADC_SG1.23, STAMP1:ADC_SG2.23, STAMP1:ADC_TEMP.23, STAMP2:ADC_SG1.23, STAMP2:ADC_SG2.23, STAMP2:ADC_TEMP.23, STAMP3:ADC_SG1.23, STAMP3:ADC_SG2.23, STAMP3:ADC_TEMP.23, STAMP4:ADC_SG1.23, STAMP4:ADC_SG2.23, STAMP4:ADC_TEMP.23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
- net DAPI_CTS: now also FTDI.38; no longer U$1.38
- net DAPI_DSR: now also FTDI.36; no longer U$1.36
- net DAPI_DTR: now also FTDI.35; no longer U$1.35
- net DAPI_RTS: now also FTDI.37; no longer U$1.37
- net DAPI_RXD: now also FTDI.40; no longer U$1.40
- net DAPI_TXD: now also FTDI.39; no longer U$1.39
- net EECLK: now also FTDI.1, FT_EEPROM.2; no longer U$1.1, U$3.2
- net EECS: now also FTDI.48, FT_EEPROM.1; no longer U$1.48, U$3.1
- net EED: now also FTDI.2, FT_EEPROM.3; no longer U$1.2, U$3.3
- net F_CLK: now also S70FL.16; no longer U$4.16
- net F_CS1: now also S70FL.7; no longer U$4.7
- net F_CS2: now also S70FL.6; no longer U$4.6
- net F_MISO: now also S70FL.8; no longer U$4.8
- net F_MOSI: now also S70FL.15; no longer U$4.15
- net GND: now also C100.2, C101.1, C103.2, C104.2, C105.2, C106.1, C108.2, C109.2, C111.2, C112.1, C113.2, C114.2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; no longer STAMP1:ADC_SG1.10, STAMP1:ADC_SG1.2, STAMP1:ADC_SG1.21, STAMP1:ADC_SG2.10, STAMP1:ADC_SG2.2, STAMP1:ADC_SG2.21, STAMP1:ADC_TEMP.10, STAMP1:ADC_TEMP.2, STAMP1:ADC_TEMP.21, STAMP1:ADC_TEMP.3, STAMP1:C28.2, STAMP1:C29.2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
- net N$11: now also FTDI.8; no longer U$1.8
- net N$12: now also FTDI.43; no longer U$1.43
- net N$13: now also FTDI.6; no longer U$1.6
- net N$14: now also FTDI.46; no longer U$1.46
- net N$15: now also FTDI.4; no longer U$1.4
- net N$18: now also FTDI.24; no longer U$1.24
- net N$19: now also FTDI.23; no longer U$1.23
- net N$20: now also FTDI.22; no longer U$1.22
- net N$21: now also FTDI.21; no longer U$1.21
- net N$22: now also FTDI.44; no longer U$1.44
- net N$23: now also FT_EEPROM.4; no longer U$3.4
- net N$8: now also FTDI.5; no longer U$1.5
- net N$9: now also FTDI.7; no longer U$1.7
- net SG_CLK: now also STAMP1_ADC_SG1.3, STAMP1_ADC_SG10.3, STAMP1_ADC_SG11.3, STAMP1_ADC_SG12.3, STAMP1_ADC_SG15.3, STAMP1_ADC_SG16.3, STAMP1_ADC_SG2.3, STAMP1_ADC_SG5.3, STAMP1_ADC_SG6.3, STAMP1_ADC_SG7.3, STAMP1_ADC_SG8.3, STAMP1_ADC_SG9.3; no longer STAMP1:ADC_SG1.3, STAMP1:ADC_SG2.3, STAMP2:ADC_SG1.3, STAMP2:ADC_SG2.3, STAMP3:ADC_SG1.3, STAMP3:ADC_SG2.3, STAMP4:ADC_SG1.3, STAMP4:ADC_SG2.3, STAMP5:ADC_SG1.3, STAMP5:ADC_SG2.3, STAMP6:ADC_SG1.3, STAMP6:ADC_SG2.3
- net STAMP1_CS_SG1: now also STAMP1_ADC_SG1.24; no longer STAMP1:ADC_SG1.24
- net STAMP1_CS_SG2: now also STAMP1_ADC_SG2.24; no longer STAMP1:ADC_SG2.24
- net STAMP1_CS_TEMP: now also STAMP1_ADC_TEMP.24; no longer STAMP1:ADC_TEMP.24
- net STAMP1_DRDY_SG1: now also STAMP1_ADC_SG1.25; no longer STAMP1:ADC_SG1.25
- net STAMP1_DRDY_SG2: now also STAMP1_ADC_SG2.25; no longer STAMP1:ADC_SG2.25
- net STAMP1_DRDY_TEMP: now also STAMP1_ADC_TEMP.25; no longer STAMP1:ADC_TEMP.25
- net STAMP1_MISO: now also R31.1, R70.1, R75.1; no longer STAMP1:R31.1, STAMP1:R70.1, STAMP1:R75.1
- net STAMP1_MOSI: now also STAMP1_ADC_SG1.27, STAMP1_ADC_SG2.27, STAMP1_ADC_TEMP.27; no longer STAMP1:ADC_SG1.27, STAMP1:ADC_SG2.27, STAMP1:ADC_TEMP.27
- net STAMP1_SCLK: now also STAMP1_ADC_SG1.28, STAMP1_ADC_SG2.28, STAMP1_ADC_TEMP.28; no longer STAMP1:ADC_SG1.28, STAMP1:ADC_SG2.28, STAMP1:ADC_TEMP.28
- net STAMP2_CS_SG1: now also STAMP1_ADC_SG5.24; no longer STAMP2:ADC_SG1.24
- net STAMP2_CS_SG2: now also STAMP1_ADC_SG6.24; no longer STAMP2:ADC_SG2.24
- net STAMP2_CS_TEMP: now also STAMP1_ADC_TEMP2.24; no longer STAMP2:ADC_TEMP.24
- net STAMP2_DRDY_SG1: now also STAMP1_ADC_SG5.25; no longer STAMP2:ADC_SG1.25
- net STAMP2_DRDY_SG2: now also STAMP1_ADC_SG6.25; no longer STAMP2:ADC_SG2.25
- net STAMP2_DRDY_TEMP: now also STAMP1_ADC_TEMP2.25; no longer STAMP2:ADC_TEMP.25
- net STAMP2_MISO: now also R83.1, R89.1, R93.1; no longer STAMP2:R31.1, STAMP2:R70.1, STAMP2:R75.1
- net STAMP2_MOSI: now also STAMP1_ADC_SG5.27, STAMP1_ADC_SG6.27, STAMP1_ADC_TEMP2.27; no longer STAMP2:ADC_SG1.27, STAMP2:ADC_SG2.27, STAMP2:ADC_TEMP.27
- net STAMP2_SCLK: now also STAMP1_ADC_SG5.28, STAMP1_ADC_SG6.28, STAMP1_ADC_TEMP2.28; no longer STAMP2:ADC_SG1.28, STAMP2:ADC_SG2.28, STAMP2:ADC_TEMP.28
- net STAMP3_CS_SG1: now also STAMP1_ADC_SG9.24; no longer STAMP3:ADC_SG1.24
- net STAMP3_CS_SG2: now also STAMP1_ADC_SG10.24; no longer STAMP3:ADC_SG2.24
- net STAMP3_CS_TEMP: now also STAMP1_ADC_TEMP4.24; no longer STAMP3:ADC_TEMP.24
- net STAMP3_DRDY_SG1: now also STAMP1_ADC_SG9.25; no longer STAMP3:ADC_SG1.25
- net STAMP3_DRDY_SG2: now also STAMP1_ADC_SG10.25; no longer STAMP3:ADC_SG2.25
- net STAMP3_DRDY_TEMP: now also STAMP1_ADC_TEMP4.25; no longer STAMP3:ADC_TEMP.25
- net STAMP3_MISO: now also R121.1, R127.1, R131.1; no longer STAMP3:R31.1, STAMP3:R70.1, STAMP3:R75.1
- net STAMP3_MOSI: now also STAMP1_ADC_SG10.27, STAMP1_ADC_SG9.27, STAMP1_ADC_TEMP4.27; no longer STAMP3:ADC_SG1.27, STAMP3:ADC_SG2.27, STAMP3:ADC_TEMP.27
- net STAMP3_SCLK: now also STAMP1_ADC_SG10.28, STAMP1_ADC_SG9.28, STAMP1_ADC_TEMP4.28; no longer STAMP3:ADC_SG1.28, STAMP3:ADC_SG2.28, STAMP3:ADC_TEMP.28
- net STAMP4_CS_SG1: now also STAMP1_ADC_SG11.24; no longer STAMP4:ADC_SG1.24
- net STAMP4_CS_SG2: now also STAMP1_ADC_SG12.24; no longer STAMP4:ADC_SG2.24
- net STAMP4_CS_TEMP: now also STAMP1_ADC_TEMP5.24; no longer STAMP4:ADC_TEMP.24
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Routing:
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- added copper zone on layer 1, net 3V3
- added copper zone on layer 16, net 3V3
- added copper zone on layer 2, net GND

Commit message: Pre DRC
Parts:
- moved C8 3.14 mm to (132.6, 79.5)
- moved C16 2.54 mm to (97.8, 78.9)
- moved R45 1.55 mm to (99.1, 73.8)
- moved C12 1.27 mm to (113.0, 57.1)
- moved R46 1.14 mm to (99.2, 73.7)
- moved C9 0.25 mm to (123.4, 87.1)
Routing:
- net GND: track 325.3 -> 1145.9 mm, vias 3 -> 54
- net SG_CLK: track 276.4 -> 446.6 mm, vias 12 -> 15
- net STAMP4_CS_SG1: track 0.00 -> 156.4 mm, vias 0 -> 4
- net STAMP3_CS_SG1: track 0.00 -> 149.4 mm, vias 0 -> 5
- net STAMP1_CS_SG1: track 0.00 -> 147.9 mm, vias 0 -> 1
- net STAMP3_DRDY_SG1: track 0.00 -> 131.9 mm, vias 0 -> 5
- net STAMP5_CS_SG1: track 0.00 -> 130.1 mm, vias 0 -> 2
- net STAMP6_DRDY_SG1: track 0.00 -> 129.4 mm, vias 0 -> 1
- net STAMP4_MOSI: track 72.6 -> 200.0 mm, vias 2 -> 4
- net STAMP6_CS_SG1: track 0.00 -> 125.0 mm, vias 0 -> 2
- net STAMP1_DRDY_SG1: track 0.00 -> 123.4 mm, vias 0 -> 2
- net STAMP1_MISO: track 28.6 -> 149.0 mm, vias 0 -> 3
- net ADC_START: track 419.3 -> 539.6 mm, vias 18 -> 21
- net STAMP1_SCLK: track 66.2 -> 185.8 mm, vias 5 -> 6
- net STAMP4_MISO: track 28.6 -> 146.4 mm, vias 0 -> 7
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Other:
- board text added: "HERMESS SPU Rev 3.0"

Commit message: Post DRC
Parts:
- moved R16 2.00 mm to (146.1, 70.6)
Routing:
- net 3V3: track 352.6 -> 364.1 mm, vias 9 -> 18
- net GND: track 1145.9 -> 1152.3 mm, vias 54 -> 59
- net 5V-28V: track 63.7 -> 67.0 mm
- net STAMP1_DRDY_TEMP: track 134.3 -> 131.0 mm
- net EXP_IN_P: track 40.2 -> 43.3 mm
- net STAMP1_CS_SG1: track 147.9 -> 149.8 mm
- net EXP_OUT: track 20.4 -> 22.0 mm
- net ADC_START: track 539.6 -> 538.0 mm
- net N$172: track 6.35 -> 7.21 mm
- net STAMP5_CS_SG2: track 95.1 -> 94.3 mm
- net EXP_IN: track 12.1 -> 12.8 mm
- net 28VGND: track 175.0 -> 174.4 mm
- net STAMP1_SCLK: track 185.8 -> 186.3 mm
- net 28V: track 209.9 -> 210.4 mm

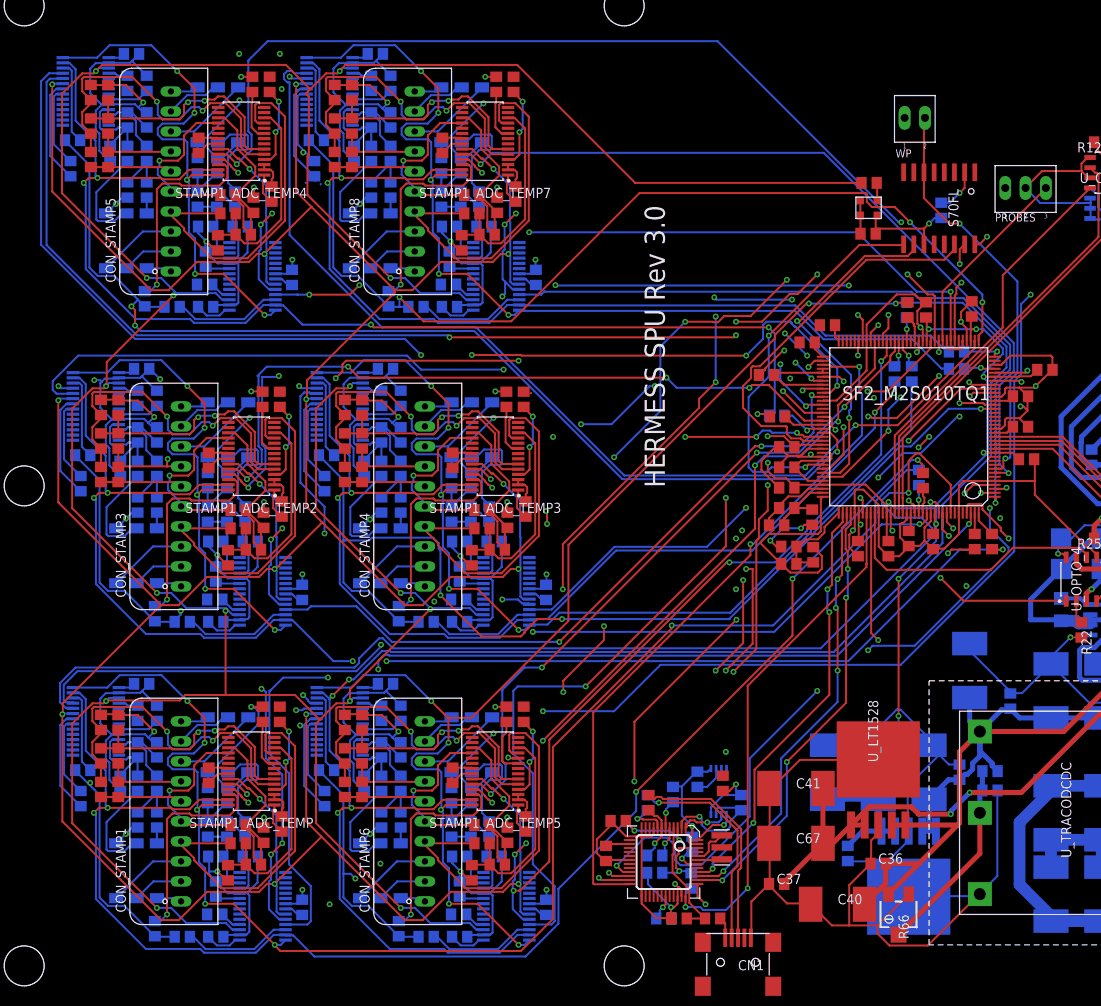
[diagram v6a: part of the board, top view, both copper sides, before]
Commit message: Finishes Airwires
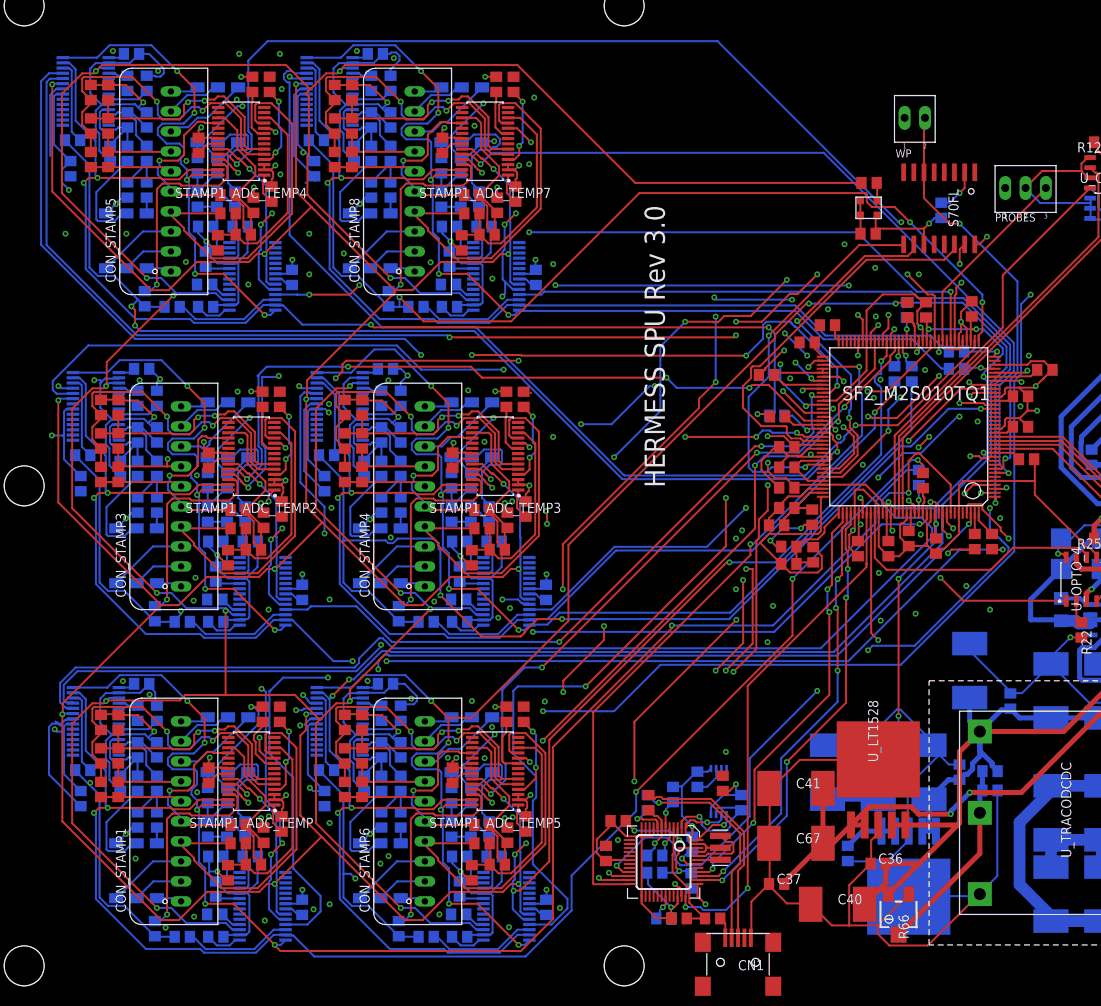
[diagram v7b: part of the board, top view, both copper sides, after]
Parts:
- moved C13 0.66 mm to (119.0, 57.5)
- moved Q2 0.18 mm to (92.0, 19.8)
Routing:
- net 3V3: track 364.1 -> 575.9 mm, vias 18 -> 98
- net GND: track 1152.3 -> 1239.0 mm, vias 59 -> 85
- net N$22: track 4.71 -> 7.78 mm
- net F_MISO: track 50.5 -> 52.3 mm
- net STAMP4_DRDY_SG2: track 110.1 -> 111.8 mm
- net N$212: track 26.3 -> 28.0 mm
- net N$209: track 13.4 -> 14.8 mm
- net N$170: track 26.3 -> 27.8 mm
- net STAMP6_TEMP_AIN1: track 46.2 -> 47.4 mm
- net STAMP5_SCLK: track 130.2 -> 131.4 mm
- net STAMP2_CS_SG1: track 104.6 -> 105.7 mm
- net N$90: track 6.35 -> 7.36 mm
- net STAMP1_DRDY_SG2: track 132.8 -> 133.8 mm
- net STAMP4_CS_SG2: track 103.7 -> 104.6 mm
- net F_MOSI: track 43.5 -> 44.3 mm
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
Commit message: Adds production files
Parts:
- moved R35 21.7 mm to (101.0, 51.3), turned to 90 degrees
- moved C41 0.33 mm to (101.1, 27.1)
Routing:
- net N$45: track 3.23 -> 32.2 mm, vias 0 -> 2
- net STAMP1_MOSI: track 188.4 -> 161.7 mm, vias 5 -> 3
- net 3V3: track 575.9 -> 574.9 mm
